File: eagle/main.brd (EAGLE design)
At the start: 72.4 x 41.3 mm, 20 parts, among them IC1 74HC164D, IC2 74LS139D, IC3 317EMP, Q1 BSS84, Q2 BSS84, Q3 BSS84, Q4 BSS123, Q5 BSS123

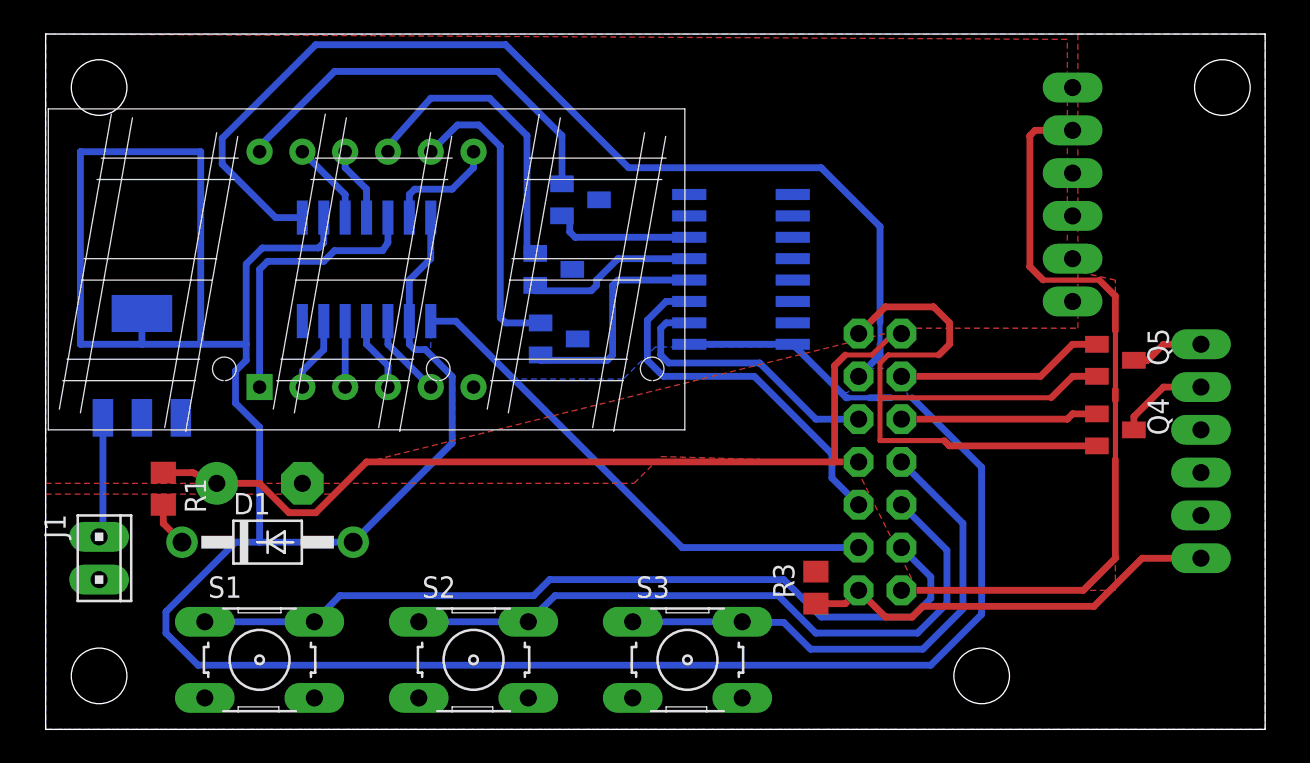
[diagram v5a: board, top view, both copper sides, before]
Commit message: Fixed up the layout a little, made the mask files consistent
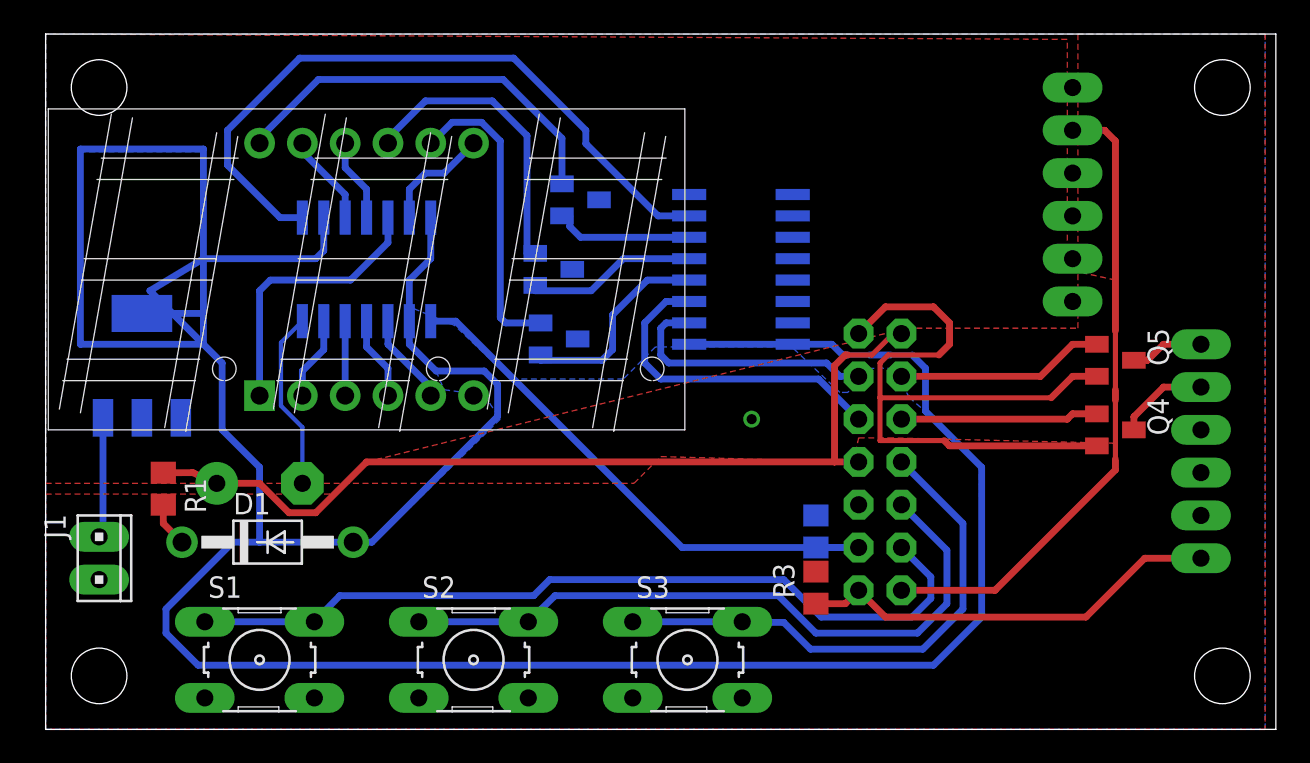
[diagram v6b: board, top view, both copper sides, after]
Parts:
- added R2: 47k, rcl:R0805
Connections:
- net GND: now also R2.2
- net N$12: now also R2.1
- net N$13: now also IC2.7; no longer 430.4
- net N$21: now also 430.6; no longer 430.10
- net N$22: now also 430.4; no longer 430.6
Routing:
- net N$13: track 62.8 -> 41.3 mm
- net VCC: track 183.1 -> 195.3 mm
- net GND: track 43.3 -> 54.0 mm, vias 0 -> 1
- net N$24: track 45.3 -> 38.0 mm
- net N$21: track 22.3 -> 19.6 mm
- net N$12: track 31.0 -> 33.5 mm
- net N$25: track 13.5 -> 12.3 mm
- net N$22: track 16.7 -> 15.7 mm
- net N$11: track 24.5 -> 23.8 mm
- net N$2: track 4.96 -> 5.47 mm
- net N$1: track 4.44 -> 4.95 mm
- net N$7: track 3.91 -> 4.42 mm
- net N$5: track 4.44 -> 4.95 mm
- net N$3: track 4.96 -> 5.47 mm
- net N$6: track 4.44 -> 4.95 mm
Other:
- board size 72.4 x 41.3 mm -> 73 x 41.3 mm

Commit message: snapshot before porting code to v4 hardware
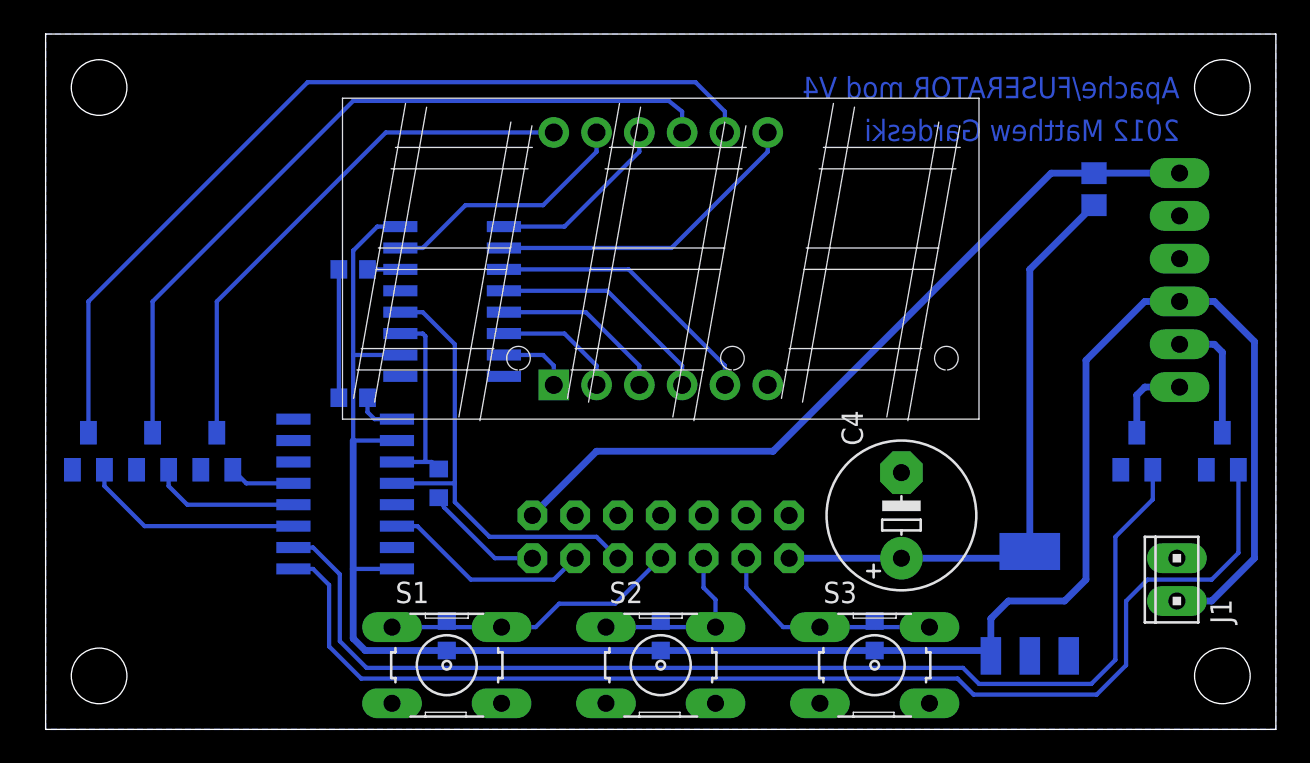
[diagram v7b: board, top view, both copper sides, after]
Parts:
- removed D1: 1N4004, diode:DO41-10
- removed IC2: 74LS139D, 74xx-us:SO16
- removed JP1: (no value), pinhead:1X06/90
- added C2, C3: (no value), rcl:C0603K
- added C4: (no value), rcl:E5-8,5
- added IC4: 74LS595D, 74xx-us:SO16
- added R4: 0, rcl:R0603
- C1: value 1F -> (none); device rcl:E5-13 -> rcl:C0603K
- IC1: value 74HC164D -> 74LS595D; device 74xx-us:SO14 -> 74xx-us:SO16
- Q1, Q2, Q3: value BSS84 -> BSS123
- R1: value 3ish -> 0; device rcl:R0805 -> rcl:R0603
- R2: value 47k -> 0; device rcl:R0805 -> rcl:R0603
- moved J1 64.0 mm to (67.2, 8.89), turned to 90 degrees
- moved IC3 54.6 mm to (58.4, 7.46)
- moved C1 37.6 mm to (49.2, 5.56), turned to 270 degrees
- moved Q1 32.8 mm to (2.54, 16.5), turned to 0 degrees
- moved R2 31.6 mm to (18.3, 27.3), turned to 180 degrees
- moved R3 28.8 mm to (62.2, 32.1), flipped to the bottom, turned to 270 degrees
- moved Q2 26.1 mm to (6.35, 16.5), turned to 0 degrees
- moved Q3 21.4 mm to (10.2, 16.5), turned to 0 degrees
- moved U$1 17.5 mm to (36.5, 27.9)
- moved 430 13.8 mm to (36.5, 11.4), turned to 0 degrees
- moved IC1 13.4 mm to (17.8, 14.0), turned to 90 degrees
- moved R1 12.5 mm to (18.3, 19.7), flipped to the bottom, turned to 0 degrees
- moved S2 11.1 mm to (36.5, 3.81)
- moved S1 11.1 mm to (23.8, 3.81)
- moved S3 11.1 mm to (49.2, 3.81)
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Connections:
- removed net N$30: IC3.3, J1.2
- new net +5V: C1.2, C2.2, C3.2, IC1.10, IC1.16, IC3.3, IC4.10, IC4.16, J1.2, JP2.4
- net GND: now also 430.12, C4.-, IC1.13, IC1.8, IC4.13, IC4.8, Q1.2, Q2.2, Q3.2; no longer C1.-, IC1.7, IC2.8, JP1.1, Q1.3, Q2.3, Q3.3, R2.2
- net N$1: now also IC4.15, U$1.P$8; no longer IC1.11, U$1.P$9
- net N$10: now also Q2.3; no longer Q2.2
- net N$11: now also Q3.3; no longer Q1.2
- net N$12: now also IC1.3, Q1.1; no longer 430.12, IC1.1, R2.1
- net N$13: now also 430.11, IC1.14; no longer IC1.8, IC2.7
- net N$14: now also IC4.14, R2.2; no longer 430.1, 430.8, C1.+, R1.1
- net N$15: now also 430.7, C3.1; no longer 430.11
- net N$16: now also IC1.9, R1.1; no longer 430.9, S2.1, S2.2
- net N$18: now also 430.3, C1.1; no longer 430.7
- net N$19: now also R1.2, R2.1; no longer 430.3, Q5.1
- net N$2: now also IC4.1, U$1.P$9; no longer IC1.10, U$1.P$8
- net N$20: now also IC1.1; no longer 430.5
- net N$21: now also IC1.11, IC4.11, R4.2; no longer 430.6, IC2.3
- net N$22: now also IC1.4, Q2.1; no longer 430.4, IC2.2
- net N$24: now also IC1.5, Q3.1; no longer 430.13, JP1.5
- net N$25: now also IC1.2, Q5.1; no longer IC2.4, Q3.1
- net N$26: now also 430.13, R4.1; no longer IC2.5, Q2.1
- net N$27: now also 430.9, IC1.12, IC4.12; no longer IC2.6, Q1.1
- net N$29: now also 430.5, C2.1, S2.1, S2.2; no longer D1.C, R1.2
- net N$3: now also IC4.7, U$1.P$1; no longer IC1.3, U$1.P$5
- net N$4: now also IC4.6, U$1.P$2; no longer IC1.12, U$1.P$1
- net N$5: now also IC4.5, U$1.P$3; no longer IC1.6, U$1.P$2
- net N$6: now also IC4.4; no longer IC1.4
- net N$7: now also IC4.3, U$1.P$5; no longer IC1.5, U$1.P$3
- net N$8: now also IC4.2; no longer IC1.13
- net N$9: now also Q1.3; no longer Q3.2
- net VCC: now also 430.1, C4.+; no longer D1.A, IC1.14, IC1.2, IC1.9, IC2.1, IC2.16
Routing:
- net VCC: track 195.3 -> 36.6 mm
- net +5V: track 0.00 -> 125.5 mm
- net N$20: track 11.7 -> 72.0 mm
- net N$25: track 12.3 -> 67.3 mm
- net GND: track 54.0 -> 0.00 mm, vias 1 -> 0
- net N$14: track 53.9 -> 1.95 mm
- net N$16: track 40.6 -> 2.77 mm
- net N$9: track 18.1 -> 52.9 mm
- net N$24: track 38.0 -> 3.93 mm
- net N$15: track 49.3 -> 18.3 mm
- net N$13: track 41.3 -> 12.4 mm
- net N$10: track 18.4 -> 45.6 mm
- net N$17: track 25.3 -> 46.8 mm
- net N$12: track 33.5 -> 13.2 mm
- net N$27: track 8.45 -> 27.9 mm
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- removed copper zone on layer 1, net GND
- removed copper zone on layer 1, net VCC
- removed copper zone on layer 16, net VCC
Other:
- board text added: "2012 Matthew Gardeski"
- board text added: "Apache/FUSERATOR mod V4"

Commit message: another big revamp
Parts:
- added J2: (no value), con-amp:10X02MTA
- C4: device rcl:E5-8,5 -> rcl:E2,5-7
- moved R3 37.1 mm to (32.7, 9.53), turned to 180 degrees
- moved R4 2.91 mm to (24.8, 17.1), turned to 0 degrees
- moved 430 1.91 mm to (36.5, 13.3)
- moved C4 1.27 mm to (50.8, 11.4)
- moved IC3 0.93 mm to (58.9, 8.26)
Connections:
- removed net N$27: 430.9, IC1.12, IC4.12
- new net N$30: 430.6, IC1.12, IC4.12
- new net N$31: 430.9, R3.2
- net +5V: no longer C1.2, C2.2, C3.2, IC1.10, IC1.16, IC4.10, IC4.16
- net GND: now also 430.13, J2.2; no longer 430.12
- net N$13: now also 430.14; no longer 430.11
- net N$17: now also 430.11, J2.1; no longer 430.14
- net N$26: now also 430.12; no longer 430.13
- net VCC: now also C1.2, C2.2, C3.2, IC1.10, IC1.16, IC4.10, IC4.16; no longer R3.2
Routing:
- net +5V: track 125.5 -> 53.6 mm
- net VCC: track 36.6 -> 92.6 mm
- net N$17: track 46.8 -> 10.1 mm
- net N$30: track 0.00 -> 33.6 mm
- net N$27: track 27.9 -> 0.00 mm
- net N$13: track 12.4 -> 9.09 mm
- net N$31: track 0.00 -> 2.67 mm
- net N$15: track 18.3 -> 20.9 mm
- net N$29: track 11.5 -> 13.4 mm
- net N$18: track 14.3 -> 15.6 mm
- net N$26: track 7.15 -> 7.99 mm
- net N$20: track 72.0 -> 72.6 mm
- added copper zone on layer 16, net N$27
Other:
- board text added: "FUSERATOR V5"
- board text removed: "Apache/FUSERATOR mod V4"
